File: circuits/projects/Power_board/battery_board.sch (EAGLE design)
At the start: 31 parts, among them M1-FUSE 3A, M2-FUSE 3A

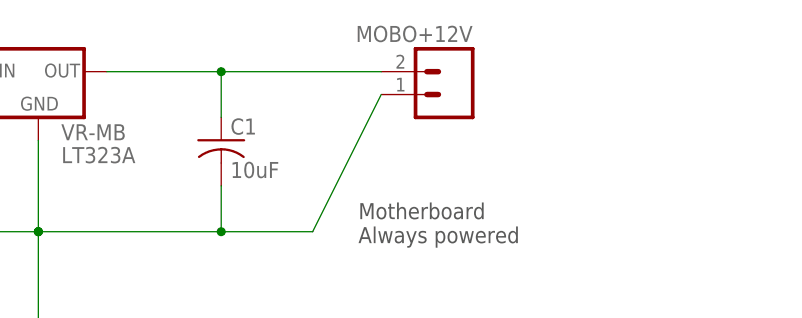
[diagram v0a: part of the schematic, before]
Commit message: battery board made
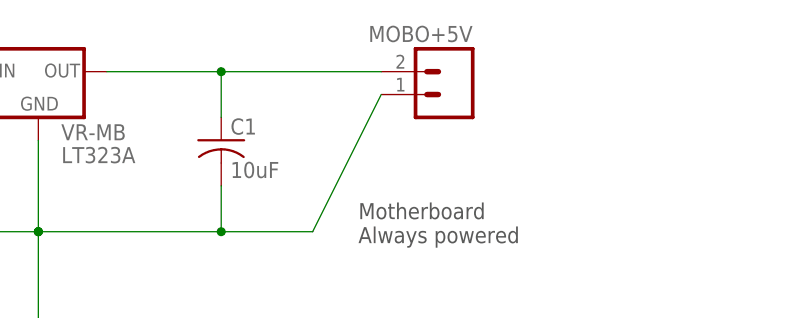
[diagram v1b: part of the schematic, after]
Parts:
- renumbered MOBO+12V to MOBO+5V
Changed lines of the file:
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@@
 <part name="D3-24V" library="parts" deviceset="NTST30100SG" device="-H" value="30A"/>
 <part name="VR-MB" library="parts" deviceset="LT323AT" device="-SINK" value="LT323A"/>
-<part name="MOBO+12V" library="parts" deviceset="2-HOLES" device="SC3.81MM"/>
+<part name="MOBO+5V" library="parts" deviceset="2-HOLES" device="SC3.81MM"/>
 <part name="C1" library="parts" deviceset="CAPACITOR" device="" value="10uF"/>
 <part name="C2" library="parts" deviceset="CAPACITOR" device="" value="2.2uF"/>
@@
 <instance part="D3-24V" gate="G$1" x="77.47" y="60.96" rot="R270"/>
 <instance part="VR-MB" gate="G$1" x="133.35" y="134.62"/>
-<instance part="MOBO+12V" gate="G$1" x="179.07" y="134.62" rot="MR0"/>
+<instance part="MOBO+5V" gate="G$1" x="179.07" y="134.62" rot="MR0"/>
 <instance part="C1" gate="G$1" x="153.67" y="127"/>
 <instance part="C2" gate="G$1" x="123.19" y="116.84" rot="R90"/>
@@
 <wire x1="133.35" y1="127" x2="133.35" y2="116.84" width="0.1524" layer="91"/>
 <junction x="133.35" y="116.84"/>
-<pinref part="MOBO+12V" gate="G$1" pin="1"/>
+<pinref part="MOBO+5V" gate="G$1" pin="1"/>
 <wire x1="171.45" y1="132.08" x2="163.83" y2="116.84" width="0.1524" layer="91"/>
 <wire x1="163.83" y1="116.84" x2="153.67" y2="116.84" width="0.1524" layer="91"/>
@@
 <net name="N$8" class="2">
 <segment>
-<pinref part="MOBO+12V" gate="G$1" pin="2"/>
+<pinref part="MOBO+5V" gate="G$1" pin="2"/>
 <pinref part="VR-MB" gate="G$1" pin="OUT"/>
 <wire x1="171.45" y1="134.62" x2="153.67" y2="134.62" width="0.1524" layer="91"/>

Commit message: first board finished
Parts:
- removed B1-FUSE, B2-FUSE: 20A, parts:FUSEBLADE
- removed M1-FUSE, M2-FUSE: 3A, parts:FUSE
- added D1: BZX55, parts:BZX55
- added FUSE-M1, FUSE-M2: 3A, parts:2-HOLESSC5MM
- D1-12V, D2-12V, D3-24V: device parts:NTST30100SG-H -> parts:POWER_RECTIFIER-H
- R1, R2, R3, R4, R5: device parts:RESISTOR0207/10 -> parts:RESISTOR0309/15
- RELAY_ON: value 1-HOLE" -> 1-HOLE; device parts:1-HOLE" -> parts:1-HOLE
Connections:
- removed net N$20: B2-FUSE.2, RELAY3.P
- removed net N$39: B1-FUSE.1, RELAY2.P
- net 24V: now also FUSE-M1.2, FUSE-M2.2; no longer M1-FUSE.2, M2-FUSE.2
- net GND: now also D1.A
- net N$1: now also RELAY2.P; no longer B1-FUSE.2
- net N$10: now also FUSE-M1.1, MOTOR-1.2; no longer M2-FUSE.1, MOTOR-2.2
- net N$15: now also D1.C
- net N$5: now also RELAY3.P; no longer B2-FUSE.1
- net N$9: now also FUSE-M2.1, MOTOR-2.2; no longer M1-FUSE.1, MOTOR-1.2
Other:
- moved on the sheet: LED-CHARGE, MOTOR-2, R5

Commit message: new boards
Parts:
- removed BATT1_V, BATT2_V, CHARGE_ON, RELAY_ON: 1-HOLE, parts:1-HOLE
- removed CHARGER: 24V, parts:2-HOLESSC5MM
- removed D1: BZX55, parts:BZX55
- removed D2-12V: 30A, parts:POWER_RECTIFIER-H
- removed LED-CHARGE, LED-CHARGING: (no value), parts:LED-5MM
- removed R1: 560R, parts:RESISTOR0309/15
- removed R4: 1k, parts:RESISTOR0309/15
- removed R5: 220R, parts:RESISTOR0309/15
- removed RELAY: 5V, parts:RT424A05
- removed VR-MB: LT323A, parts:LT323AT-SINK
- added +5V-1, +5V-2: 2-HOLESSC3.81MM, parts:2-HOLESSC3.81MM
- added C1_V1, C1_V2: 2.2uF, parts:CAPACITOR
- added C2_V1, C2_V2: 10uF, parts:CAPACITOR
- added OUTPUT-SHAFT: 3-HOLE, parts:3-HOLE
- added TEST: (no value), parts:M03PTH
- added VR-MB1, VR-MB2, VR-MB3: LT323A, parts:LT323AT-V
- renumbered C1 to C2_V3, C2 to C1_V3, MOBO+5V to +5V-3
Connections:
- removed net N$11: RELAY1.1, RELAY_ON.1
- removed net N$12: C1_V3.1, D2-12V.C, VR-MB.IN
- removed net N$13: R1.2, RELAY2.S
- removed net N$16: LED-CHARGE.A, R5.1
- removed net N$2: CHARGER.2, R4.2, RELAY3.S
- removed net N$5: BATT2_V.1, BATTERY2.+, RELAY3.P
- removed net N$6: D1-12V.A, RELAY2.O
- removed net N$7: LED-CHARGING.A, R1.1
- new net N$17: +5V-1.2, C2_V1.1, VR-MB1.OUT
- net 12V: now also C1_V1.1, C1_V2.1, C1_V3.1, OUTPUT-SHAFT.3, VR-MB1.IN, VR-MB2.IN, VR-MB3.IN
- net 24V: now also OUTPUT-SHAFT.1
- net GND: now also +5V-1.1, +5V-2.1, C1_V1.2, C1_V2.2, C2_V1.2, C2_V2.2, OUTPUT-SHAFT.2, TEST.1, VR-MB1.GND, VR-MB2.GND, VR-MB3.GND; no longer CHARGER.1, D1.A, LED-CHARGE.C, LED-CHARGING.C, RELAY1.2, VR-MB.GND
- net N$1: now also D1-12V.A, TEST.2; no longer BATT1_V.1, D2-12V.A, RELAY2.P
- net N$15: now also +5V-2.2, C2_V2.1, VR-MB2.OUT; no longer CHARGE_ON.1, D1.C, R4.1, R5.2
- net N$4: now also BATTERY2.+, TEST.3; no longer RELAY3.O
- net N$8: now also VR-MB3.OUT; no longer VR-MB.OUT
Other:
- note removed: "Battery Charger Relay switches"
- note removed: "Motherboard Always powered"

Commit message: woowoooo
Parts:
- removed VR-MB1, VR-MB2, VR-MB3: LT323A, parts:LT323AT-V
- added U$11, U$12, U$13: LD1085_3A-VREG, parts:LD1085_3A-VREG
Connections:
- net 12V: now also U$11.IN, U$12.IN, U$13.IN; no longer VR-MB1.IN, VR-MB2.IN, VR-MB3.IN
- net GND: now also U$11.GND, U$12.GND, U$13.GND; no longer VR-MB1.GND, VR-MB2.GND, VR-MB3.GND
- net N$15: now also U$12.OUT; no longer VR-MB2.OUT
- net N$17: now also U$11.OUT; no longer VR-MB1.OUT
- net N$8: now also U$13.OUT; no longer VR-MB3.OUT
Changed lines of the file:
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@@
 <setting verticaltext="up"/>
 </settings>
-<grid distance="0.1" unitdist="inch" unit="inch" style="lines" multiple="1" display="no" altdistance="0.01" altunitdist="inch" altunit="inch"/>
+<grid distance="0.05" unitdist="inch" unit="inch" style="lines" multiple="1" display="no" altdistance="0.01" altunitdist="inch" altunit="inch"/>
 <layers>
 <layer number="1" name="Top" color="4" fill="1" visible="no" active="no"/>
@@
 <layer number="54" name="bGND_GNDA" color="1" fill="9" visible="no" active="no"/>
 <layer number="56" name="wert" color="7" fill="1" visible="no" active="no"/>
+<layer number="57" name="tCAD" color="7" fill="1" visible="no" active="no"/>
 <layer number="91" name="Nets" color="2" fill="1" visible="yes" active="yes"/>
 <layer number="92" name="Busses" color="1" fill="1" visible="yes" active="yes"/>
@@
 <layer number="97" name="Info" color="9" fill="1" visible="yes" active="yes"/>
 <layer number="98" name="Guide" color="6" fill="1" visible="yes" active="yes"/>
+<layer number="99" name="SpiceOrder" color="7" fill="1" visible="yes" active="yes"/>
 <layer number="100" name="Muster" color="7" fill="1" visible="no" active="no"/>
 <layer number="101" name="Patch_Top" color="12" fill="4" visible="yes" active="yes"/>
@@
 <layer number="111" name="LPC17xx" color="7" fill="1" visible="yes" active="yes"/>
 <layer number="112" name="tSilk" color="7" fill="1" visible="yes" active="yes"/>
+<layer number="113" name="IDFDebug" color="7" fill="1" visible="yes" active="yes"/>
 <layer number="116" name="Patch_BOT" color="9" fill="4" visible="yes" active="yes"/>
 <layer number="121" name="_tsilk" color="7" fill="1" visible="yes" active="yes"/>
@@
 <layer number="132" name="bAdjust" color="7" fill="1" visible="yes" active="yes"/>
 <layer number="144" name="Drill_legend" color="7" fill="1" visible="yes" active="yes"/>
+<layer number="150" name="Notes" color="7" fill="1" visible="yes" active="yes"/>
 <layer number="151" name="HeatSink" color="7" fill="1" visible="yes" active="yes"/>
 <layer number="152" name="_bDocu" color="7" fill="1" visible="yes" active="yes"/>
+<layer number="153" name="FabDoc1" color="7" fill="1" visible="yes" active="yes"/>
+<layer number="154" name="FabDoc2" color="7" fill="1" visible="yes" active="yes"/>
+<layer number="155" name="FabDoc3" color="7" fill="1" visible="yes" active="yes"/>
 <layer number="199" name="Contour" color="7" fill="1" visible="yes" active="yes"/>
 <layer number="200" name="200bmp" color="1" fill="10" visible="yes" active="yes"/>
@@
 <part name="GND1" library="parts" deviceset="GND" device=""/>
 <part name="D3-24V" library="parts" deviceset="POWER_RECTIFIER" device="-H" value="30A"/>
-<part name="VR-MB3" library="parts" deviceset="LT323AT" device="-V" value="LT323A"/>
 <part name="+5V-3" library="parts" deviceset="2-HOLES" device="SC3.81MM"/>
 <part name="C2_V3" library="parts" deviceset="CAPACITOR" device="" value="10uF"/>
@@
 <part name="FUSE-M2" library="parts" deviceset="2-HOLES" device="SC5MM" value="3A"/>
 <part name="FUSE-M1" library="parts" deviceset="2-HOLES" device="SC5MM" value="3A"/>
-<part name="VR-MB2" library="parts" deviceset="LT323AT" device="-V" value="LT323A"/>
 <part name="+5V-2" library="parts" deviceset="2-HOLES" device="SC3.81MM"/>
 <part name="C2_V2" library="parts" deviceset="CAPACITOR" device="" value="10uF"/>
 <part name="C1_V2" library="parts" deviceset="CAPACITOR" device="" value="2.2uF"/>
-<part name="VR-MB1" library="parts" deviceset="LT323AT" device="-V" value="LT323A"/>
 <part name="+5V-1" library="parts" deviceset="2-HOLES" device="SC3.81MM"/>
 <part name="C2_V1" library="parts" deviceset="CAPACITOR" device="" value="10uF"/>
@@
 <part name="OUTPUT-SHAFT" library="parts" deviceset="3-HOLE" device=""/>
 <part name="TEST" library="parts" deviceset="M03" device="PTH"/>
+<part name="U$11" library="parts" deviceset="LD1085_3A-VREG" device=""/>
+<part name="U$12" library="parts" deviceset="LD1085_3A-VREG" device=""/>
+<part name="U$13" library="parts" deviceset="LD1085_3A-VREG" device=""/>
 </parts>
 <sheets>
@@
 <instance part="GND1" gate="1" x="153.67" y="81.28"/>
 <instance part="D3-24V" gate="G$1" x="77.47" y="60.96" rot="R270"/>
-<instance part="VR-MB3" gate="G$1" x="133.35" y="134.62"/>
 <instance part="+5V-3" gate="G$1" x="179.07" y="134.62" rot="MR0"/>
 <instance part="C2_V3" gate="G$1" x="153.67" y="127"/>
@@
 <instance part="FUSE-M2" gate="G$1" x="20.32" y="63.5" rot="R180"/>
 <instance part="FUSE-M1" gate="G$1" x="41.91" y="63.5" rot="R180"/>
-<instance part="VR-MB2" gate="G$1" x="52.07" y="134.62"/>
 <instance part="+5V-2" gate="G$1" x="97.79" y="134.62" rot="MR0"/>
 <instance part="C2_V2" gate="G$1" x="72.39" y="127"/>
 <instance part="C1_V2" gate="G$1" x="41.91" y="116.84" rot="R90"/>
-<instance part="VR-MB1" gate="G$1" x="-26.67" y="134.62"/>
 <instance part="+5V-1" gate="G$1" x="19.05" y="134.62" rot="MR0"/>
 <instance part="C2_V1" gate="G$1" x="-6.35" y="127"/>
@@
 <instance part="OUTPUT-SHAFT" gate="G$1" x="152.4" y="-13.97" rot="MR90"/>
 <instance part="TEST" gate="G$1" x="102.87" y="62.23" rot="R90"/>
+<instance part="U$11" gate="G$1" x="-26.67" y="134.62"/>
+<instance part="U$12" gate="G$1" x="52.07" y="134.62"/>
+<instance part="U$13" gate="G$1" x="133.35" y="134.62"/>
 </instances>
 <busses>
@@
 <wire x1="153.67" y1="86.36" x2="153.67" y2="83.82" width="0.1524" layer="91"/>
 <wire x1="133.35" y1="88.9" x2="153.67" y2="88.9" width="0.1524" layer="91"/>
-<pinref part="VR-MB3" gate="G$1" pin="GND"/>
 <wire x1="133.35" y1="127" x2="133.35" y2="116.84" width="0.1524" layer="91"/>
 <junction x="133.35" y="116.84"/>
@@
 <wire x1="133.35" y1="99.06" x2="133.35" y2="88.9" width="0.1524" layer="91"/>
 <wire x1="128.27" y1="88.9" x2="133.35" y2="88.9" width="0.1524" layer="91"/>
-<pinref part="VR-MB2" gate="G$1" pin="GND"/>
 <wire x1="52.07" y1="127" x2="52.07" y2="116.84" width="0.1524" layer="91"/>
 <junction x="52.07" y="116.84"/>
@@
 <wire x1="52.07" y1="99.06" x2="52.07" y2="116.84" width="0.1524" layer="91"/>
 <junction x="133.35" y="99.06"/>
-<pinref part="VR-MB1" gate="G$1" pin="GND"/>
 <wire x1="-26.67" y1="127" x2="-26.67" y2="116.84" width="0.1524" layer="91"/>
 <junction x="-26.67" y="116.84"/>
@@
 <pinref part="TEST" gate="G$1" pin="1"/>
 <wire x1="105.41" y1="69.85" x2="106.68" y2="69.85" width="0.1524" layer="91"/>
+<pinref part="U$11" gate="G$1" pin="GND"/>
+<pinref part="U$12" gate="G$1" pin="GND"/>
+<pinref part="U$13" gate="G$1" pin="GND"/>
 </segment>
 <segment>
@@
 <segment>
 <pinref part="+5V-3" gate="G$1" pin="2"/>
-<pinref part="VR-MB3" gate="G$1" pin="OUT"/>
 <wire x1="171.45" y1="134.62" x2="153.67" y2="134.62" width="0.1524" layer="91"/>
 <pinref part="C2_V3" gate="G$1" pin="1"/>
@@
 <wire x1="153.67" y1="129.54" x2="153.67" y2="134.62" width="0.1524" layer="91"/>
 <junction x="153.67" y="134.62"/>
+<pinref part="U$13" gate="G$1" pin="OUT"/>
 </segment>
 </net>
@@
 <segment>
 <pinref part="+5V-2" gate="G$1" pin="2"/>
-<pinref part="VR-MB2" gate="G$1" pin="OUT"/>
 <wire x1="90.17" y1="134.62" x2="72.39" y2="134.62" width="0.1524" layer="91"/>
 <pinref part="C2_V2" gate="G$1" pin="1"/>
@@
 <wire x1="72.39" y1="129.54" x2="72.39" y2="134.62" width="0.1524" layer="91"/>
 <junction x="72.39" y="134.62"/>
+<pinref part="U$12" gate="G$1" pin="OUT"/>
 </segment>
 </net>
@@
 <segment>
 <pinref part="+5V-1" gate="G$1" pin="2"/>
-<pinref part="VR-MB1" gate="G$1" pin="OUT"/>
 <wire x1="11.43" y1="134.62" x2="-6.35" y2="134.62" width="0.1524" layer="91"/>
 <pinref part="C2_V1" gate="G$1" pin="1"/>
@@
 <wire x1="-6.35" y1="129.54" x2="-6.35" y2="134.62" width="0.1524" layer="91"/>
 <junction x="-6.35" y="134.62"/>
+<pinref part="U$11" gate="G$1" pin="OUT"/>
 </segment>
 </net>
 <net name="12V" class="2">
 <segment>
-<pinref part="VR-MB3" gate="G$1" pin="IN"/>
 <wire x1="118.11" y1="134.62" x2="125.73" y2="134.62" width="0.1524" layer="91"/>
 <wire x1="118.11" y1="116.84" x2="118.11" y2="134.62" width="0.1524" layer="91"/>
@@
 <junction x="118.11" y="116.84"/>
 <junction x="118.11" y="110.49"/>
-<pinref part="VR-MB2" gate="G$1" pin="IN"/>
 <wire x1="36.83" y1="134.62" x2="44.45" y2="134.62" width="0.1524" layer="91"/>
 <wire x1="36.83" y1="116.84" x2="36.83" y2="134.62" width="0.1524" layer="91"/>
@@
 <wire x1="36.83" y1="110.49" x2="36.83" y2="116.84" width="0.1524" layer="91"/>
 <junction x="36.83" y="116.84"/>
-<pinref part="VR-MB1" gate="G$1" pin="IN"/>
 <wire x1="-41.91" y1="134.62" x2="-34.29" y2="134.62" width="0.1524" layer="91"/>
 <wire x1="-41.91" y1="116.84" x2="-41.91" y2="134.62" width="0.1524" layer="91"/>
@@
 <pinref part="OUTPUT-SHAFT" gate="G$1" pin="3"/>
 <wire x1="154.94" y1="-6.35" x2="154.94" y2="0" width="0.1524" layer="91"/>
-</segment>
-</net>
+<pinref part="U$11" gate="G$1" pin="IN"/>
+<pinref part="U$12" gate="G$1" pin="IN"/>
+<pinref part="U$13" gate="G$1" pin="IN"/>
+</segment>
+</net>

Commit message: zippity boo
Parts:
- removed D1-12V: 30A, parts:POWER_RECTIFIER-H
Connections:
- removed net N$1: BATTERY1.+, BATTERY2.-, D1-12V.A, TEST.2
- removed net N$4: BATTERY2.+, D3-24V.A, TEST.3
- new net N$5: BATTERY1.+, BATTERY2.-, R3.1, TEST.2
- net 12V: now also BATTERY2.+, D3-24V.A, TEST.3; no longer D1-12V.C, OUTPUT-SHAFT.3, OUTPUT.3, R3.1
- net 24V: now also OUTPUT-SHAFT.3, OUTPUT.3
